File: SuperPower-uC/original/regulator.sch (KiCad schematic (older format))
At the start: 45 parts, among them Q10 2N7002A, Q11 2N7002A, Q13 DMP2035UVT, Q14 DMP2035UVT, Q5 DMP2035UVT, Q9 2N7002A, U10 TPS63070RNMT, U9 TPS63070RNMT

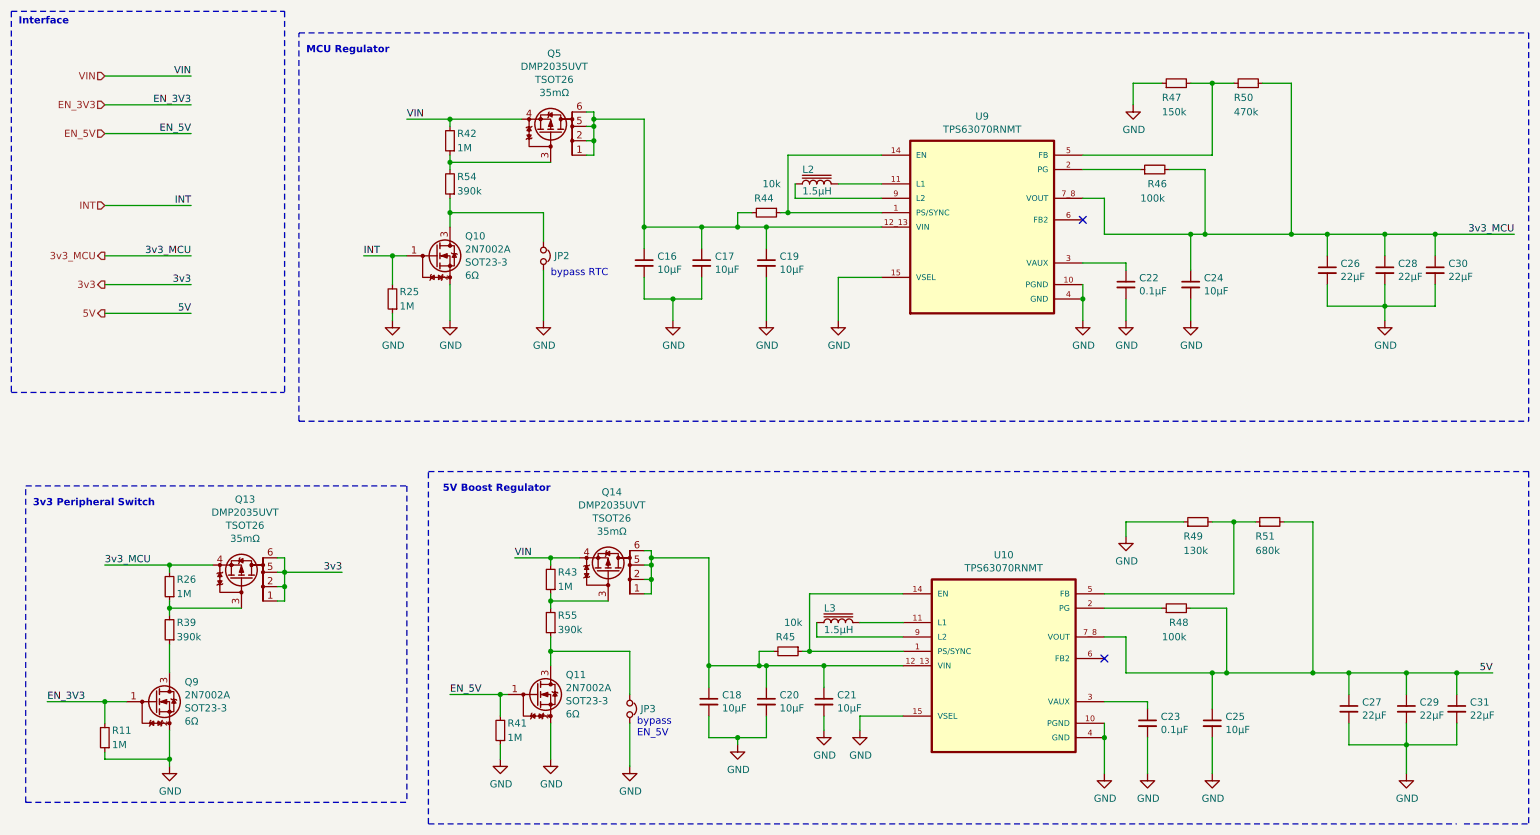
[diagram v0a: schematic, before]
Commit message: Update Single rows Headers to be fully compatible with ESP WROOM modules
(ESP-32 DevKit C rev. 4)
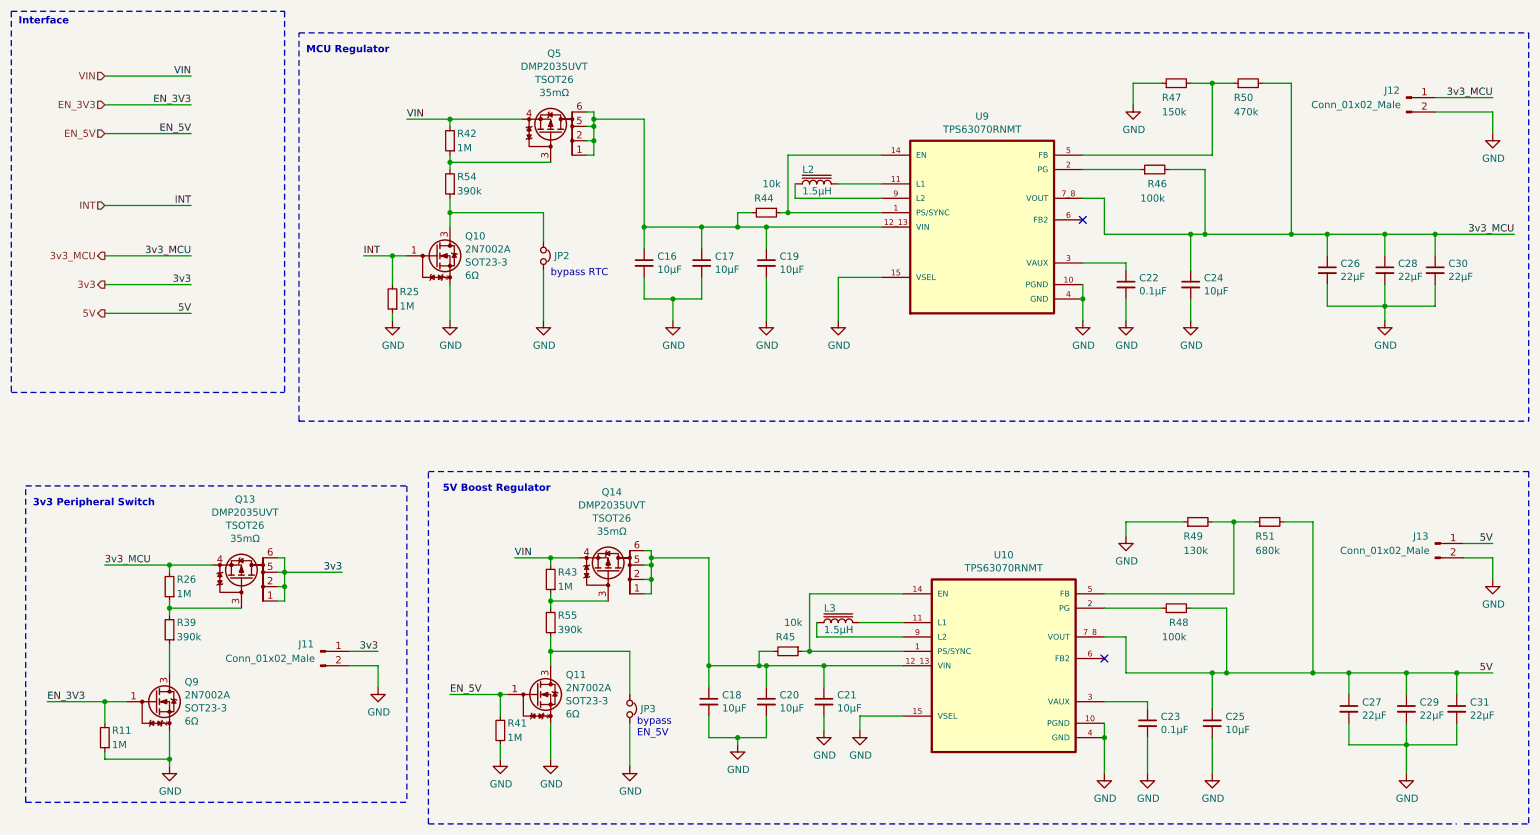
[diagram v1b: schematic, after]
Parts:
- added J11, J12, J13: Conn_01x02_Male, Connector_PinSocket_2.54mm:PinSocket_1x02_P2.54mm_Vertical, symbol Connector:Conn_01x02_Male
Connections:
- net 3v3: now also J11.1 (Pin_1)
- net 3v3_MCU: now also J12.1 (Pin_1)
- net 5V: now also J13.1 (Pin_1)
- net GND: now also J11.2 (Pin_2), J12.2 (Pin_2), J13.2 (Pin_2)
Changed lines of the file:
@@
 Wire Wire Line
 	3200 2250 3000 2250
+$Comp
+L Connector:Conn_01x02_Male J?
+U 1 1 5FE9C0CB
+P 10450 4250
+AR Path="/5F63A00B/5FE9C0CB" Ref="J?"  Part="1"
+AR Path="/5F63A0E9/5FE9C0CB" Ref="J13"  Part="1"
+F 0 "J13" H 10350 4300 50  0000 C CNN
+F 1 "Conn_01x02_Male" H 10100 4200 50  0000 C CNN
+F 2 "Connector_PinSocket_2.54mm:PinSocket_1x02_P2.54mm_Vertical" H 10450 4250 50  0001 C CNN
+F 3 "~" H 10450 4250 50  0001 C CNN
+	1    10450 4250
+	1    0    0    -1
+$EndComp
+Wire Wire Line
+	10650 4250 10850 4250
+Wire Wire Line
+	10650 4350 10850 4350
+$Comp
+L power:GND #PWR040
+U 1 1 5FEC3738
+P 10850 4500
+F 0 "#PWR040" H 10850 4250 50  0001 C CNN
+F 1 "GND" H 10855 4327 50  0000 C CNN
+F 2 "" H 10850 4500 50  0001 C CNN
+F 3 "" H 10850 4500 50  0001 C CNN
+	1    10850 4500
+	1    0    0    -1
+$EndComp
+Wire Wire Line
+	10850 4350 10850 4500
+Text Label 10850 4250 2    50   ~ 0
+5V
+$Comp
+L Connector:Conn_01x02_Male J?
+U 1 1 5FED3368
+P 10250 1150
+AR Path="/5F63A00B/5FED3368" Ref="J?"  Part="1"
+AR Path="/5F63A0E9/5FED3368" Ref="J12"  Part="1"
+F 0 "J12" H 10150 1200 50  0000 C CNN
+F 1 "Conn_01x02_Male" H 9900 1100 50  0000 C CNN
+F 2 "Connector_PinSocket_2.54mm:PinSocket_1x02_P2.54mm_Vertical" H 10250 1150 50  0001 C CNN
+F 3 "~" H 10250 1150 50  0001 C CNN
+	1    10250 1150
+	1    0    0    -1
+$EndComp
+Wire Wire Line
+	10450 1150 10850 1150
+Wire Wire Line
+	10450 1250 10850 1250
+$Comp
+L power:GND #PWR022
+U 1 1 5FED3370
+P 10850 1400
+F 0 "#PWR022" H 10850 1150 50  0001 C CNN
+F 1 "GND" H 10855 1227 50  0000 C CNN
+F 2 "" H 10850 1400 50  0001 C CNN
+F 3 "" H 10850 1400 50  0001 C CNN
+	1    10850 1400
+	1    0    0    -1
+$EndComp
+Wire Wire Line
+	10850 1250 10850 1400
+Text Label 10850 1150 2    50   ~ 0
+3v3_MCU
+$Comp
+L Connector:Conn_01x02_Male J?
+U 1 1 5FEEEF8D
+P 2700 5000
+AR Path="/5F63A00B/5FEEEF8D" Ref="J?"  Part="1"
+AR Path="/5F63A0E9/5FEEEF8D" Ref="J11"  Part="1"
+F 0 "J11" H 2600 5050 50  0000 C CNN
+F 1 "Conn_01x02_Male" H 2350 4950 50  0000 C CNN
+F 2 "Connector_PinSocket_2.54mm:PinSocket_1x02_P2.54mm_Vertical" H 2700 5000 50  0001 C CNN
+F 3 "~" H 2700 5000 50  0001 C CNN
+	1    2700 5000
+	1    0    0    -1
+$EndComp
+Wire Wire Line
+	2900 5000 3100 5000
+Wire Wire Line
+	2900 5100 3100 5100
+$Comp
+L power:GND #PWR014
+U 1 1 5FEEEF95
+P 3100 5250
+F 0 "#PWR014" H 3100 5000 50  0001 C CNN
+F 1 "GND" H 3105 5077 50  0000 C CNN
+F 2 "" H 3100 5250 50  0001 C CNN
+F 3 "" H 3100 5250 50  0001 C CNN
+	1    3100 5250
+	1    0    0    -1
+$EndComp
+Wire Wire Line
+	3100 5100 3100 5250
+Text Label 3100 5000 2    50   ~ 0
+3v3
 $EndSCHEMATC

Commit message: Update Placement + Add some labels
+3.3V Buck-Boost DC-DC converter
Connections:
- net 3v3_EN: now reaches R44.1, U9.1 (PS/SYNC), U9.14 (EN)
- net 3v3_L1: now reaches L2.2, U9.11 (L1)
- net 3v3_Vin: now reaches C16.1, C17.1, C19.1, Q5.1 (D), Q5.2 (D), Q5.5 (D), Q5.6 (D), R44.2, U9.12_13 (VIN)
- net 3v3_PG: now reaches R46.1, U9.2 (PG)
- net 3v3_Vaux: now reaches C22.1, U9.3 (VAUX)
- net 3v3_FB: now reaches R47.2, R50.1, U9.5 (FB)
- net 3v3_L2: now reaches L2.1, U9.9 (L2)
- net 3v3_OnOff_Gate: now reaches Q5.3 (G), R42.1, R54.2
- net 3v3_OnOff: now reaches JP2.1, Q10.3 (D), R54.1
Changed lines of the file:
@@
 Text Label 3100 5000 2    50   ~ 0
 3v3
+Text Label 6200 2050 0    50   ~ 0
+3v3_Vin
+Text Label 8050 1550 0    50   ~ 0
+3v3_FB
+Text Label 8050 1650 0    50   ~ 0
+3v3_PG
+Text Label 6350 1850 0    50   ~ 0
+3v3_L2
+Text Label 6350 1750 0    50   ~ 0
+3v3_L1
+Text Label 3800 1950 0    50   ~ 0
+3v3_OnOff
+Text Label 8050 2300 0    50   ~ 0
+3v3_Vaux
+Text Label 6250 1550 0    50   ~ 0
+3v3_EN
+Text Label 3700 1600 0    50   ~ 0
+3v3_OnOff_Gate
 $EndSCHEMATC

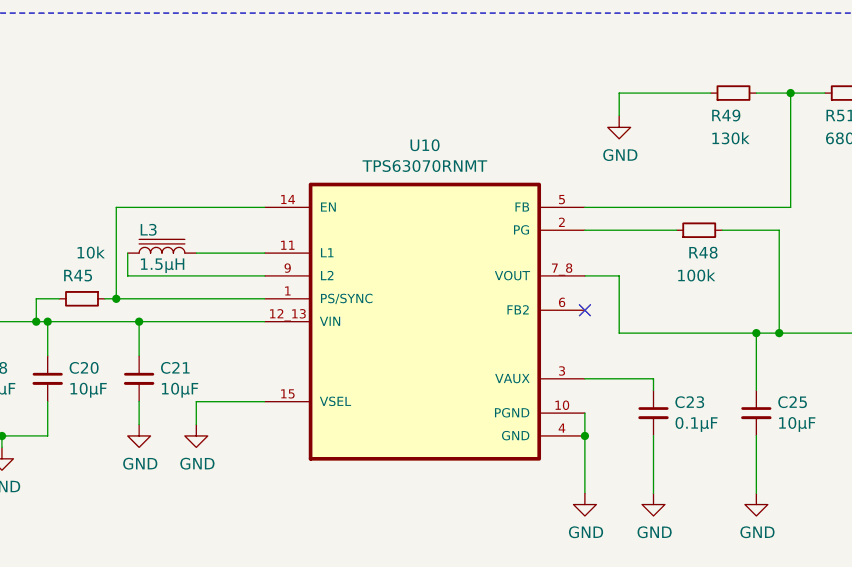
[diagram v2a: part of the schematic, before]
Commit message: Update components Placement
+5V Buck-Boost + Misc.
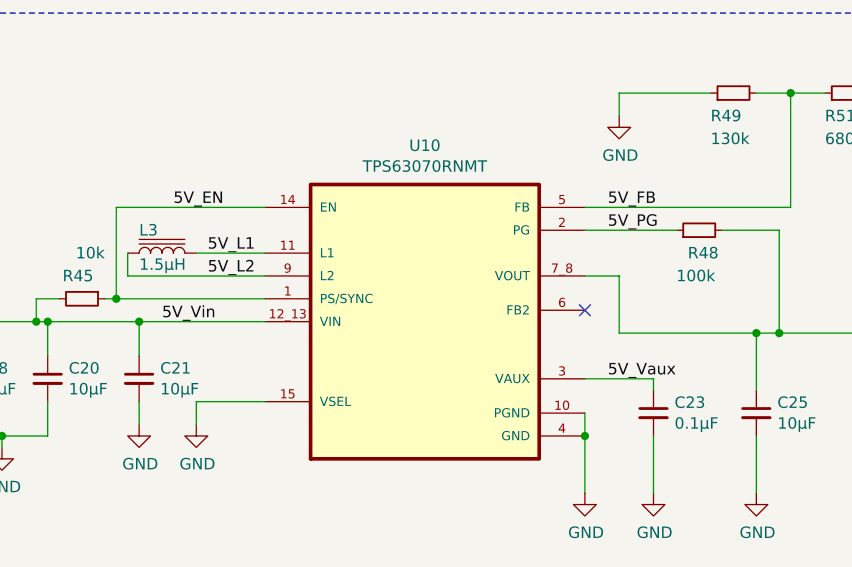
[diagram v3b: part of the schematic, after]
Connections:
- net 5V_L2: now reaches L3.1, U10.9 (L2)
- net 5V_L1: now reaches L3.2, U10.11 (L1)
- net 5V_Vin: now reaches C18.1, C20.1, C21.1, Q14.1 (D), Q14.2 (D), Q14.5 (D), Q14.6 (D), R45.2, U10.12_13 (VIN)
- net 5V_EN: now reaches R45.1, U10.1 (PS/SYNC), U10.14 (EN)
- net 5V_PG: now reaches R48.1, U10.2 (PG)
- net 5V_FB: now reaches R49.2, R51.1, U10.5 (FB)
- net 5V_Vaux: now reaches C23.1, U10.3 (VAUX)
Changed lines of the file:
@@
 Text Label 3700 1600 0    50   ~ 0
 3v3_OnOff_Gate
+Text Label 6350 4600 0    50   ~ 0
+5V_EN
+Text Label 6300 5100 0    50   ~ 0
+5V_Vin
+Text Label 6500 4800 0    50   ~ 0
+5V_L1
+Text Label 6500 4900 0    50   ~ 0
+5V_L2
+Text Label 8250 4600 0    50   ~ 0
+5V_FB
+Text Label 8250 4700 0    50   ~ 0
+5V_PG
+Text Label 8250 5350 0    50   ~ 0
+5V_Vaux
 $EndSCHEMATC

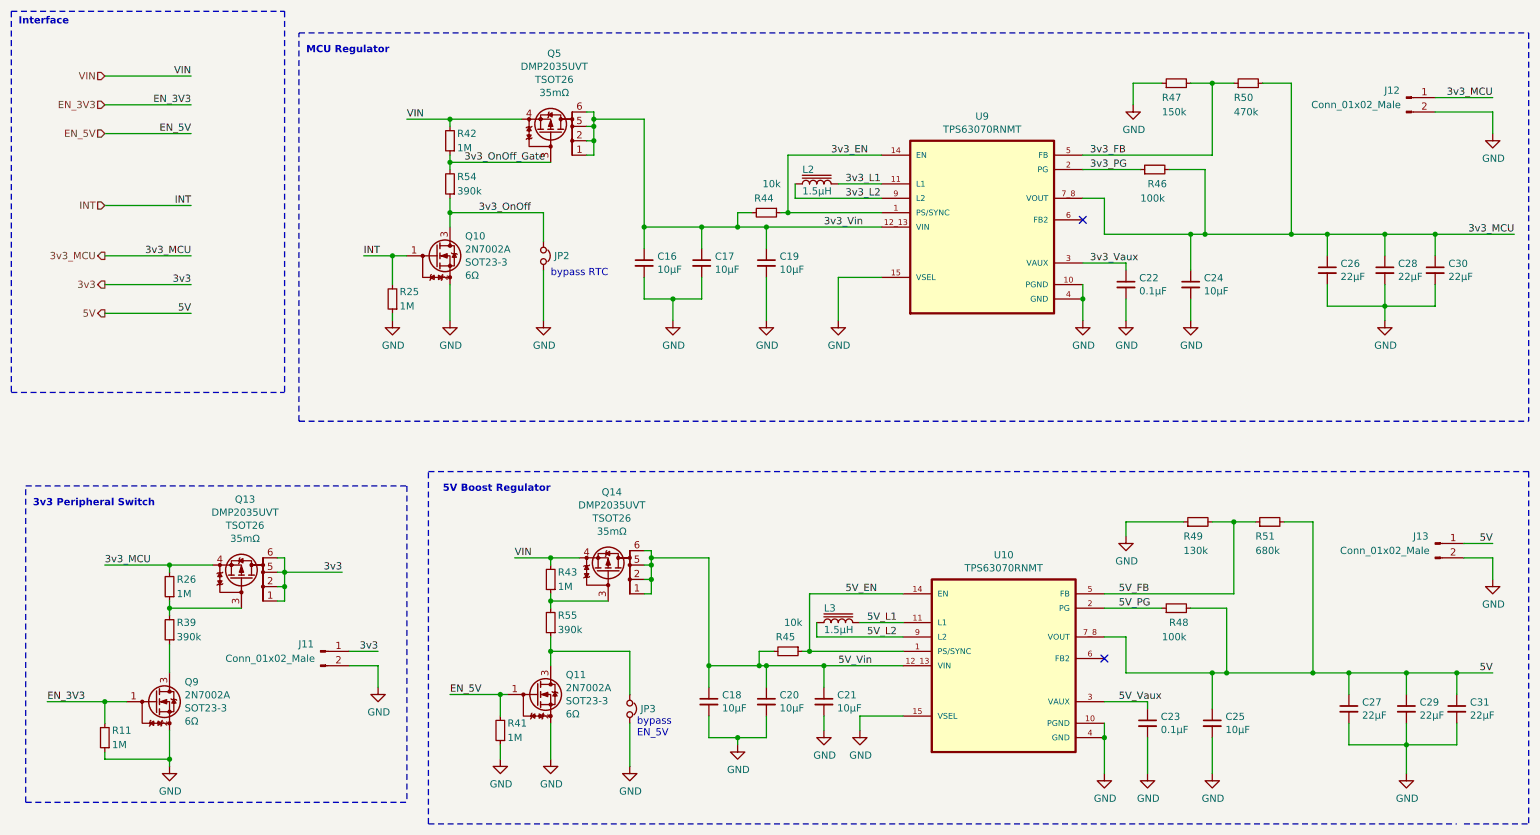
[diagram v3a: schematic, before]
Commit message: Add some DIP switch 1 way (x3)
+ add optionnal on board 0603 NTC + misc.
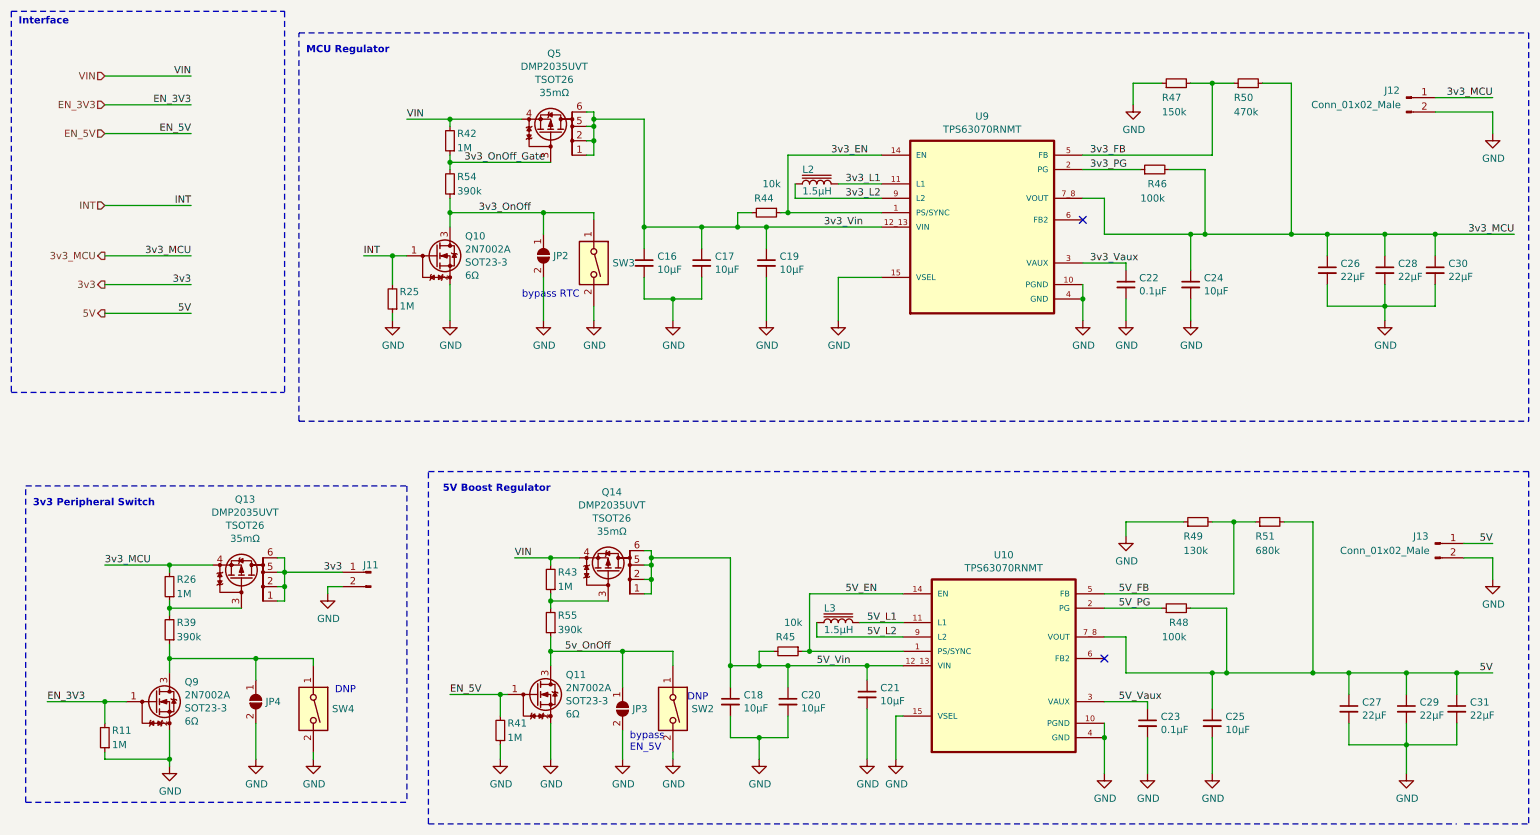
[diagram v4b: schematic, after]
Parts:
- removed JP2: Jumper_NC_Small, Connector_PinSocket_2.54mm:PinSocket_1x02_P2.54mm_Vertical, symbol Device:Jumper_NC_Small
- removed JP3: Jumper_NC_Small, Jumper:SolderJumper-2_P1.3mm_Open_TrianglePad1.0x1.5mm, symbol Device:Jumper_NC_Small
- added JP2, JP3, JP4: SolderJumper_2_Open, Jumper:SolderJumper-2_P1.3mm_Open_TrianglePad1.0x1.5mm, symbol Jumper:SolderJumper_2_Open
- added SW2, SW3, SW4: SW_DIP_x01, Button_Switch_SMD:SW_DIP_SPSTx01_Slide_Copal_CHS-01A_W5.08mm_P1.27mm_JPin, symbol Switch:SW_DIP_x01
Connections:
- net 3v3_OnOff: now also JP2.1 (A), SW3.1
- net GND: now also JP2.2 (B), JP3.2 (B), JP4.2 (B), SW2.2, SW3.2, SW4.2
- net 5v_OnOff: now reaches Q11.3 (D), R55.1
- net 5v_OnOff: now also JP3.1 (A), SW2.1
- net at Q9.3 (D), R39.1: now also JP4.1 (A), SW4.1
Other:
- note added: "DNP\n"
- moved on the sheet: C18, C20, C21, J11
